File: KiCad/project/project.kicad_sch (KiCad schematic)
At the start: 25 parts, among them P1 TerminalBlock 5P 5.0mm, U1 DRV8313PWPR

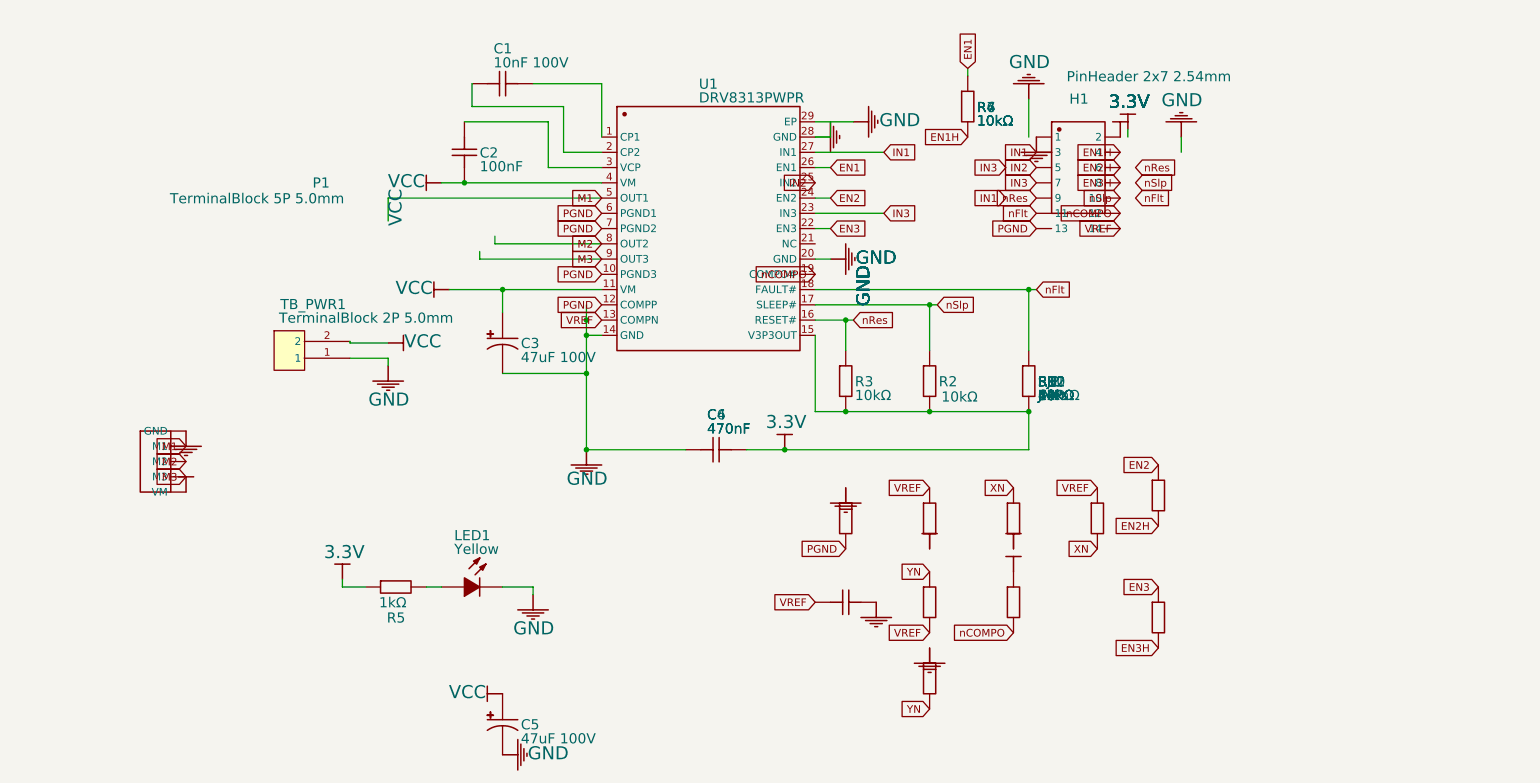
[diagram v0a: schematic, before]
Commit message: Redo schematic layout.
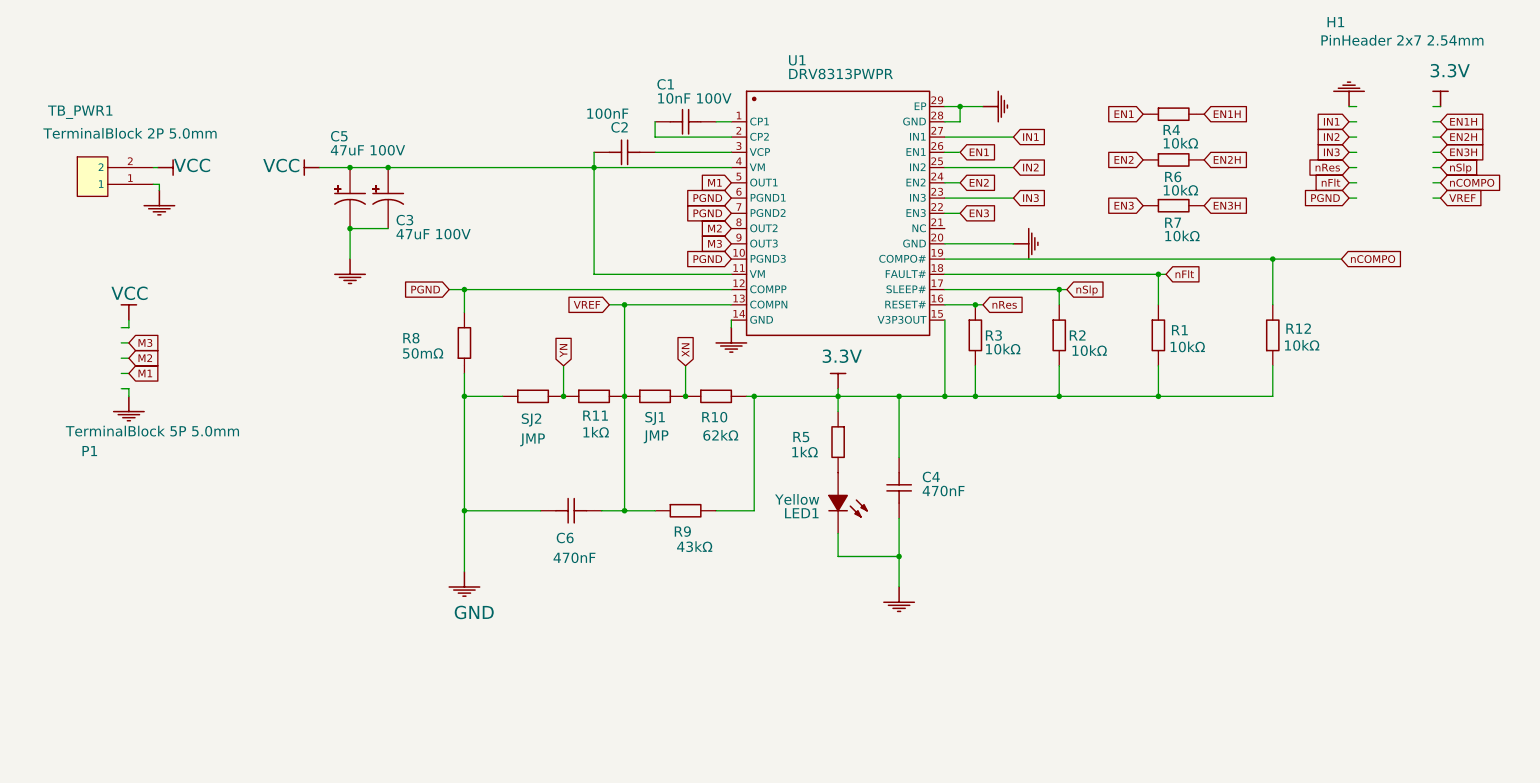
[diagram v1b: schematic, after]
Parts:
- H1: symbol Female header2.54mm2*5p Straight -> Connector_Generic:Conn_02x07_Odd_Even
- P1: symbol Header-Female-2.54_1x3 -> Connector_Generic:Conn_01x05
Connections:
- net 3.3V: no longer H1.2
- net EN1H: no longer H1.4
- net EN2H: no longer H1.6
- net EN3H: no longer H1.8
- net GND: no longer H1.1, P1.1 (GND)
- net IN1: no longer H1.3
- net IN2: no longer H1.5
- net IN3: no longer H1.7
- net M1: no longer P1.2 (M1)
- net M2: no longer P1.3 (M2)
- net M3: no longer P1.4 (M3)
- net PGND: no longer H1.13
- net VCC: no longer P1.5 (VM)
- net VREF: no longer H1.14
- net nCOMPO: no longer H1.12
- net nFlt: no longer H1.11
- net nRes: no longer H1.9
- net nSlp: no longer H1.10
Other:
- moved on the sheet: C1, C2, C3, C4, C5, C6, LED1, R1, R10, R11, R12, R2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
